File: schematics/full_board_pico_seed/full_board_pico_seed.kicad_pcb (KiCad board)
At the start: 4 copper layers, 128.3 x 74.9 mm, 136 parts, among them J1 XLR3, J10 Conn_02x03_Odd_Even, J2 Conn_01x02_Pin, J3 XLR3, J4 Aux In, J5 Conn_01x03_Female, J6 XLR3, J7 Conn_02x20_Odd_Even, J8 Conn_01x03, J9 Conn_01x02_Male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

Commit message: updated schematic
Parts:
- moved U10 15.2 mm to (155.4, 132.3), turned to -90 degrees
- moved TP9 9.14 mm to (164.3, 88.4)
- moved J5 5.17 mm to (165.1, 66.2), turned to -90 degrees
- moved TP8 5.08 mm to (155.7, 90.4)
- moved J4 5.05 mm to (123.4, 66.2), turned to -90 degrees
- moved TP10 3.18 mm to (142.7, 101.6)
- moved C9 1.08 mm to (128.4, 79.8), turned to 0 degrees
- moved C13 1.03 mm to (119.1, 81.6), turned to 90 degrees
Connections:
- C10 pad 2: Net-(J4-Pin_1) -> Net-(J4-Pin_2)
- C13 pad 1: GND -> Net-(U3A--)
- C13 pad 2: Net-(U3A--) -> /Analog Preamp/Left Analog Out
- C16 pad 2: Net-(J5-Pin_2) -> Net-(J5-Pin_3)
- C19 pad 2: Net-(J5-Pin_3) -> Net-(J5-Pin_2)
- C8 pad 2: Net-(J4-Pin_2) -> Net-(J4-Pin_3)
- C9 pad 1: GND -> Net-(U3D--)
- C9 pad 2: Net-(U3D--) -> /Analog Preamp/Right Analog Out
- J10 pad 1: Net-(J10-Pin_1) -> /UI Controller/prog_miso
- J10 pad 3: Net-(J10-Pin_3) -> /UI Controller/prog_sck
- J10 pad 4: Net-(J10-Pin_4) -> /UI Controller/prog_mosi
- J10 pad 5: Net-(J10-Pin_5) -> /UI Controller/prog_reset
- J4 pad 1: Net-(J4-Pin_1) -> GND
- J4 pad 3: GND -> Net-(J4-Pin_3)
- J7 pad 15: unconnected-(J7-Pin_15-Pad15) -> /UI Controller/prog_miso
- J7 pad 17: unconnected-(J7-Pin_17-Pad17) -> /UI Controller/prog_reset
- J7 pad 6: Net-(J7-Pin_6) -> /UI Controller/prog_mosi
- J7 pad 8: Net-(J7-Pin_8) -> /UI Controller/prog_sck
- J8 pad 1: Net-(J8-Pin_1) -> GND
- J8 pad 2: GND -> Net-(J8-Pin_2)
- R32 pad 1: Net-(J8-Pin_1) -> Net-(J8-Pin_2)
- R33 pad 2: Net-(J8-Pin_1) -> Net-(J8-Pin_2)
- R34 pad 2: Net-(J10-Pin_5) -> /UI Controller/prog_reset
- U10 pad 1: Net-(J7-Pin_4) -> GND
- U10 pad 2: Net-(J7-Pin_6) -> 3V3
- U10 pad 3: Net-(J7-Pin_8) -> Net-(J7-Pin_12)
- U10 pad 5: Net-(J7-Pin_12) -> /UI Controller/prog_sck
- U10 pad 6: 3V3 -> /UI Controller/prog_mosi
- U10 pad 7: GND -> Net-(J7-Pin_4)
- U7 pad 15: Net-(J10-Pin_4) -> /UI Controller/prog_mosi
- U7 pad 16: Net-(J10-Pin_1) -> /UI Controller/prog_miso
- U7 pad 17: Net-(J10-Pin_3) -> /UI Controller/prog_sck
- U7 pad 29: Net-(J10-Pin_5) -> /UI Controller/prog_reset
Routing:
- net /UI Controller/prog_reset: track 0.00 -> 112.6 mm, vias 0 -> 1
- net /UI Controller/prog_sck: track 0.00 -> 83.3 mm, vias 0 -> 2
- net /UI Controller/prog_mosi: track 0.00 -> 82.7 mm, vias 0 -> 1
- net /UI Controller/prog_miso: track 0.00 -> 78.3 mm, vias 0 -> 1
- net Net-(J10-Pin_5): track 30.1 -> 0.00 mm, vias 1 -> 0
- net Net-(J7-Pin_8): track 29.3 -> 0.00 mm
- net Net-(J7-Pin_6): track 29.3 -> 0.00 mm
- net Net-(J10-Pin_4): track 18.4 -> 0.00 mm
- net Net-(J10-Pin_3): track 13.8 -> 0.00 mm, vias 1 -> 0
- net 3V3: track 128.1 -> 141.3 mm, vias 6 -> 4
- net Net-(J10-Pin_1): track 13.1 -> 0.00 mm
- net /Codec/codec_sdin: track 63.8 -> 72.8 mm
- net Net-(J4-Pin_3): track 0.00 -> 8.66 mm
- net Net-(J8-Pin_2): track 0.00 -> 6.46 mm
- net Net-(J8-Pin_1): track 6.46 -> 0.00 mm
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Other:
- board text added: "3.3V"
- board text added: "5V Dig."
- board text added: "Enc. A"
- board text added: "Enc. B"
- board text added: "FreeStompFX Full Board V0.2.0"
- board text added: "Green"
- board text added: "I2C SCL"
- board text added: "I2C SDA"
- board text added: "P1"
- board text added: "P2"
- board text added: "P3"
- board text added: "Red"
- board text added: "SPI miso"
- board text added: "SPI mosi"
- board text added: "SPI sck"
- board text added: "bicolor LED"
- board text added: "codec lrclk"
- board text added: "codec reset"
- board text added: "codec sclk"
- board text added: "codec sdin"
- board text added: "codec sdout"
- board text added: "display CS"
- board text added: "display d/c"
- board text added: "display rst"
- board text added: "led clipIn"
- board text added: "led clipOut"
- board text added: "prog reset"
- board text added: "switch enter"
- board text added: "switch exit"
- board text added: "wiring"
- board text removed: "PiPicoFX Full Board V0.1.1"

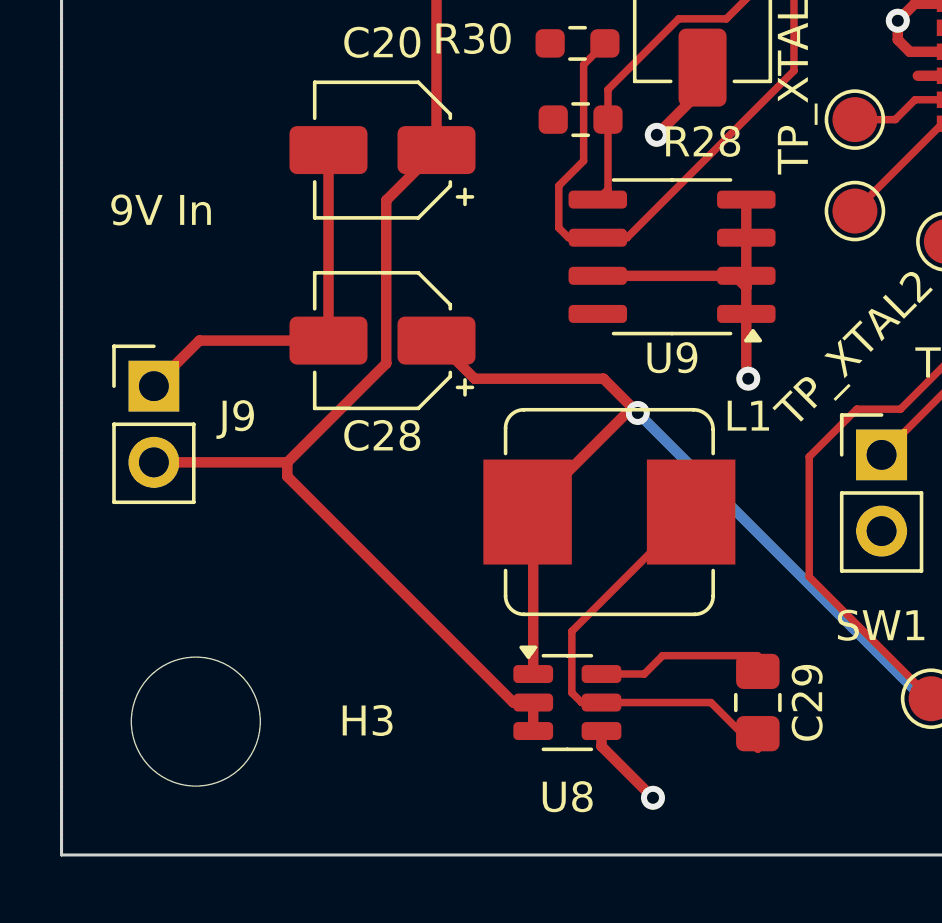
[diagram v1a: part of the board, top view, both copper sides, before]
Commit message: avr flasher: schematic changes
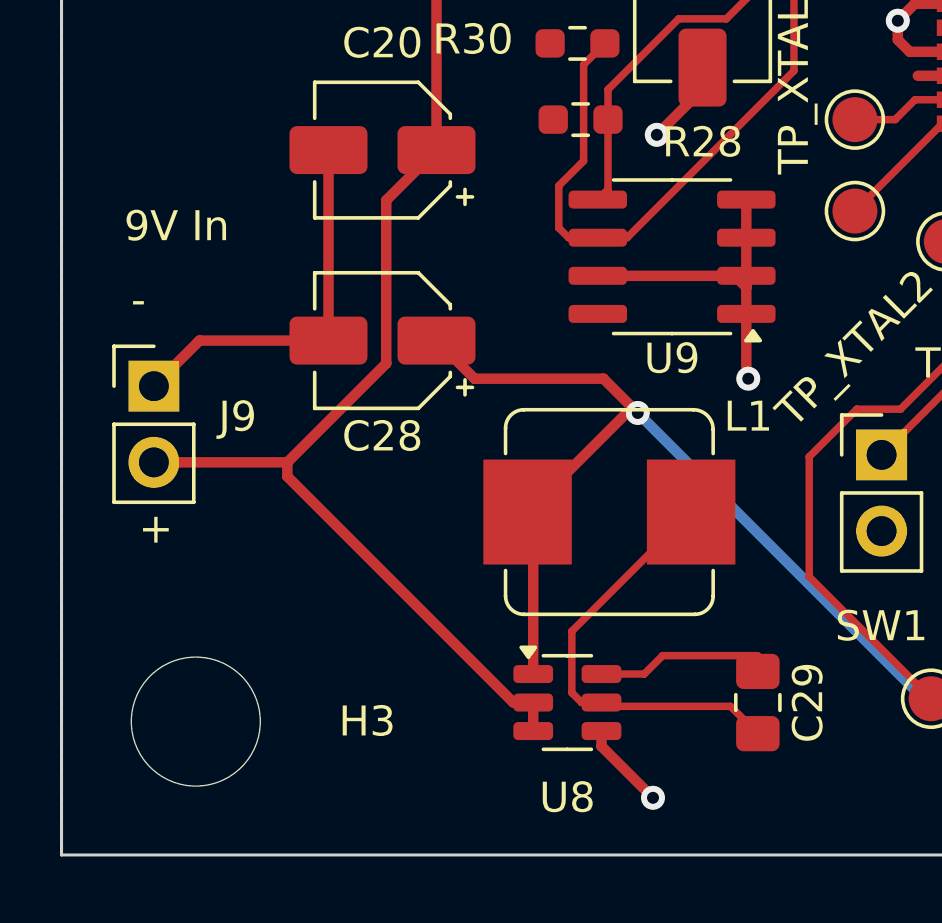
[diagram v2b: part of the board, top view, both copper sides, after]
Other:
- board text added: "+"
- board text added: "-"
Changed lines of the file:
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@@
 		(tags "Through hole pin header THT 1x03 2.54mm single row")
 		(property "Reference" "J5"
-			(at 1.905 -3.175 360)
+			(at 1.905 -3.175 0)
 			(layer "F.SilkS")
 			(hide yes)
@@
 		)
 		(fp_text user "${REFERENCE}"
-			(at 0 2.54 360)
+			(at 0 2.54 0)
 			(layer "F.Fab")
 			(effects
@@
 		(tags "Through hole pin header THT 1x03 2.54mm single row")
 		(property "Reference" "J4"
-			(at 0.635 7.62 360)
+			(at 0.635 7.62 0)
 			(layer "F.SilkS")
 			(effects
@@
 		)
 		(fp_text user "${REFERENCE}"
-			(at 0 2.54 360)
+			(at 0 2.54 0)
 			(layer "F.Fab")
 			(effects
@@
 		(tags "Through hole pin header THT 1x07 2.54mm single row")
 		(property "Reference" "U10"
-			(at 0 -3.175 360)
+			(at 0 -3.175 0)
 			(layer "F.SilkS")
 			(effects
@@
 		)
 		(fp_text user "${REFERENCE}"
-			(at 0 7.62 360)
+			(at 0 7.62 0)
 			(layer "F.Fab")
 			(effects
@@
 		)
 	)
+	(gr_text "+"
+		(at 72.39 127.508 0)
+		(layer "F.SilkS")
+		(effects
+			(font
+				(size 1 1)
+				(thickness 0.15)
+			)
+			(justify left bottom)
+		)
+	)
 	(gr_text "I2C SCL"
 		(at 157.226 98.552 90)
@@
 	)
 	(gr_text "9V In"
-		(at 73.152 116.332 0)
+		(at 73.66 116.84 0)
 		(layer "F.SilkS")
 		(effects
@@
 		)
 	)
+	(gr_text "-"
+		(at 72.136 119.888 0)
+		(layer "F.SilkS")
+		(effects
+			(font
+				(size 1 1)
+				(thickness 0.15)
+			)
+			(justify left bottom)
+		)
+	)
 	(gr_text "5V Dig."
 		(at 147.066 114.808 90)
@@
 	(segment
 		(start 87.8175 132.715)
-		(end 91.4675 132.715)
+		(end 87.9445 132.842)
 		(width 0.25)
 		(layer "F.Cu")
@@
 	)
 	(segment
-		(start 86.83 132.389999)
-		(end 87.155001 132.715)
+		(start 87.9445 132.842)
+		(end 92.1195 132.842)
 		(width 0.25)
 		(layer "F.Cu")
@@
 	)
 	(segment
-		(start 90.805 126.365)
-		(end 86.83 130.34)
+		(start 92.1195 132.842)
+		(end 93.03 133.7525)
 		(width 0.25)
 		(layer "F.Cu")
@@
 	)
 	(segment
-		(start 91.4675 132.715)
-		(end 93.03 134.2775)
+		(start 86.83 132.389999)
+		(end 87.155001 132.715)
+		(width 0.25)
+		(layer "F.Cu")
+		(net 64)
+	)
+	(segment
+		(start 90.805 126.365)
+		(end 86.83 130.34)
 		(width 0.25)
 		(layer "F.Cu")
